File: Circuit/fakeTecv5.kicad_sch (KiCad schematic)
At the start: 33 parts, among them J11 FET1 3,3, J12 FET2 3,3, J13 FET3 3,3, J14 GPS Pins, J16 Encoder Pads, J5 I2C Oled screen, J6 FET1 Drain, J7 FET2 Drain, J8 FET3 Drain, J9 Battery Connector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

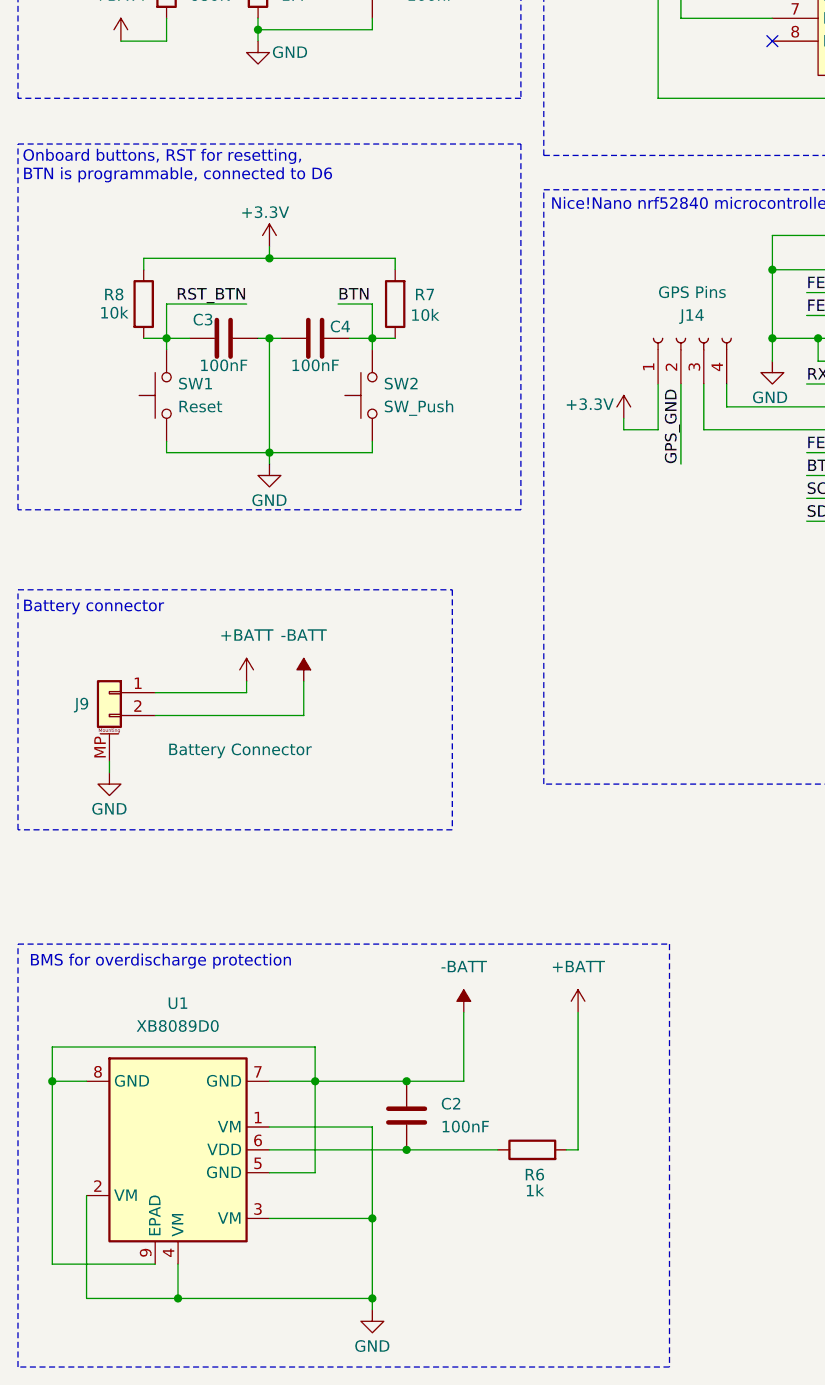
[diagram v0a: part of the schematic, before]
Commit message: Added pads for nice!nano and nrf promicro, more deco, more justifications
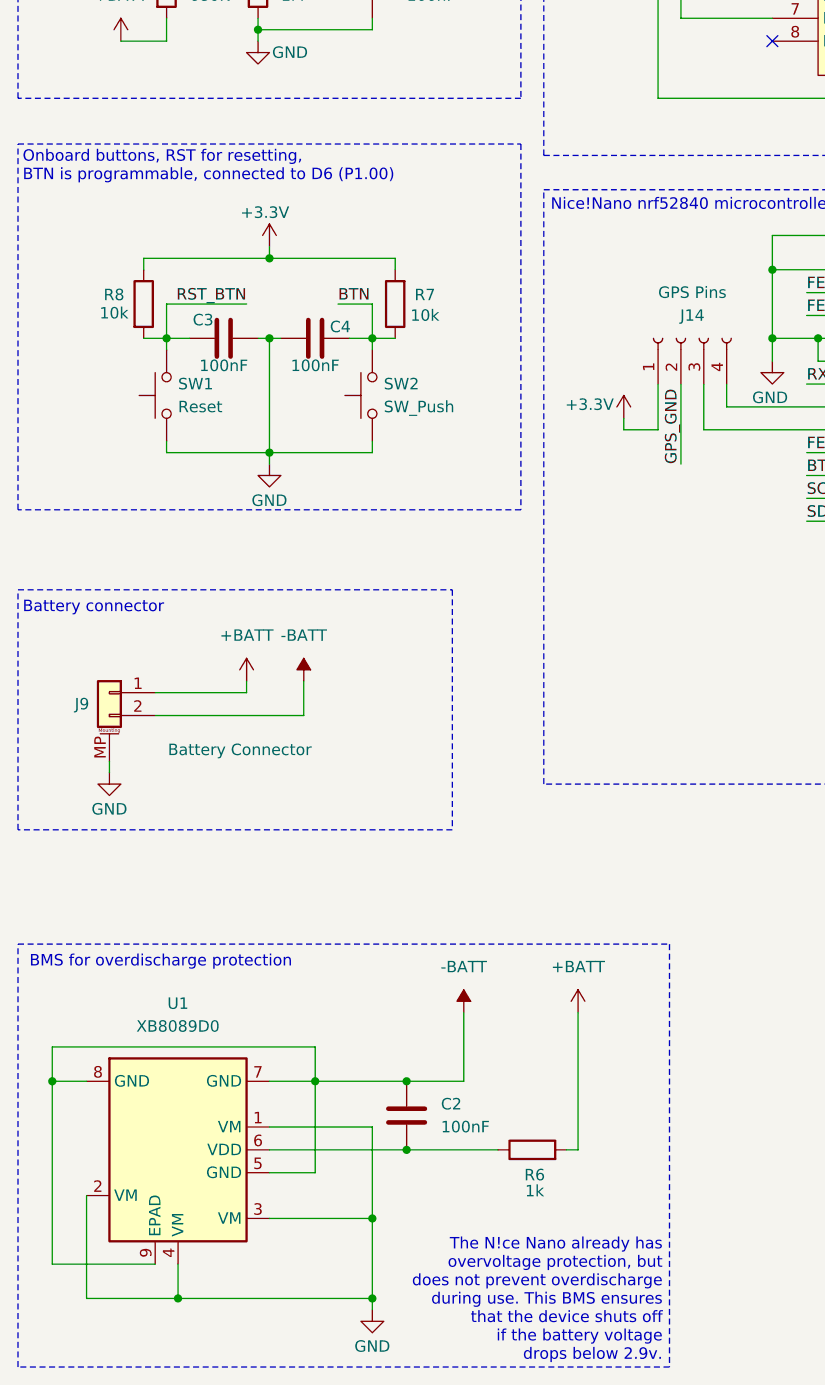
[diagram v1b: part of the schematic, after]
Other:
- note added: "Onboard buttons, RST for resetting, BTN is programmable, connected to D6 (P1.00)"
- note added: "The N!ce Nano already has overvoltage protection, but does not prevent overdischarge during use. This BMS ensures that the device shuts off if the battery voltage drops below 2.9v."
- note removed: "Onboard buttons, RST for resetting, BTN is programmable, connected to D6"
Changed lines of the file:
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@@
+		)
+	)
+	(text "The N!ce Nano already has\novervoltage protection, but\ndoes not prevent overdischarge\nduring use. This BMS ensures\nthat the device shuts off \nif the battery voltage \ndrops below 2.9v."
+		(exclude_from_sim no)
+		(at 90.678 189.992 0)
+		(effects
+			(font
+				(size 1.27 1.27)
+			)
+			(justify right bottom)
 		)
 	)
@@
 		)
 	)
-	(text "Onboard buttons, RST for resetting,\nBTN is programmable, connected to D6"
+	(text "Onboard buttons, RST for resetting,\nBTN is programmable, connected to D6 (P1.00)"
 		(exclude_from_sim no)
 		(at 19.558 57.15 0)

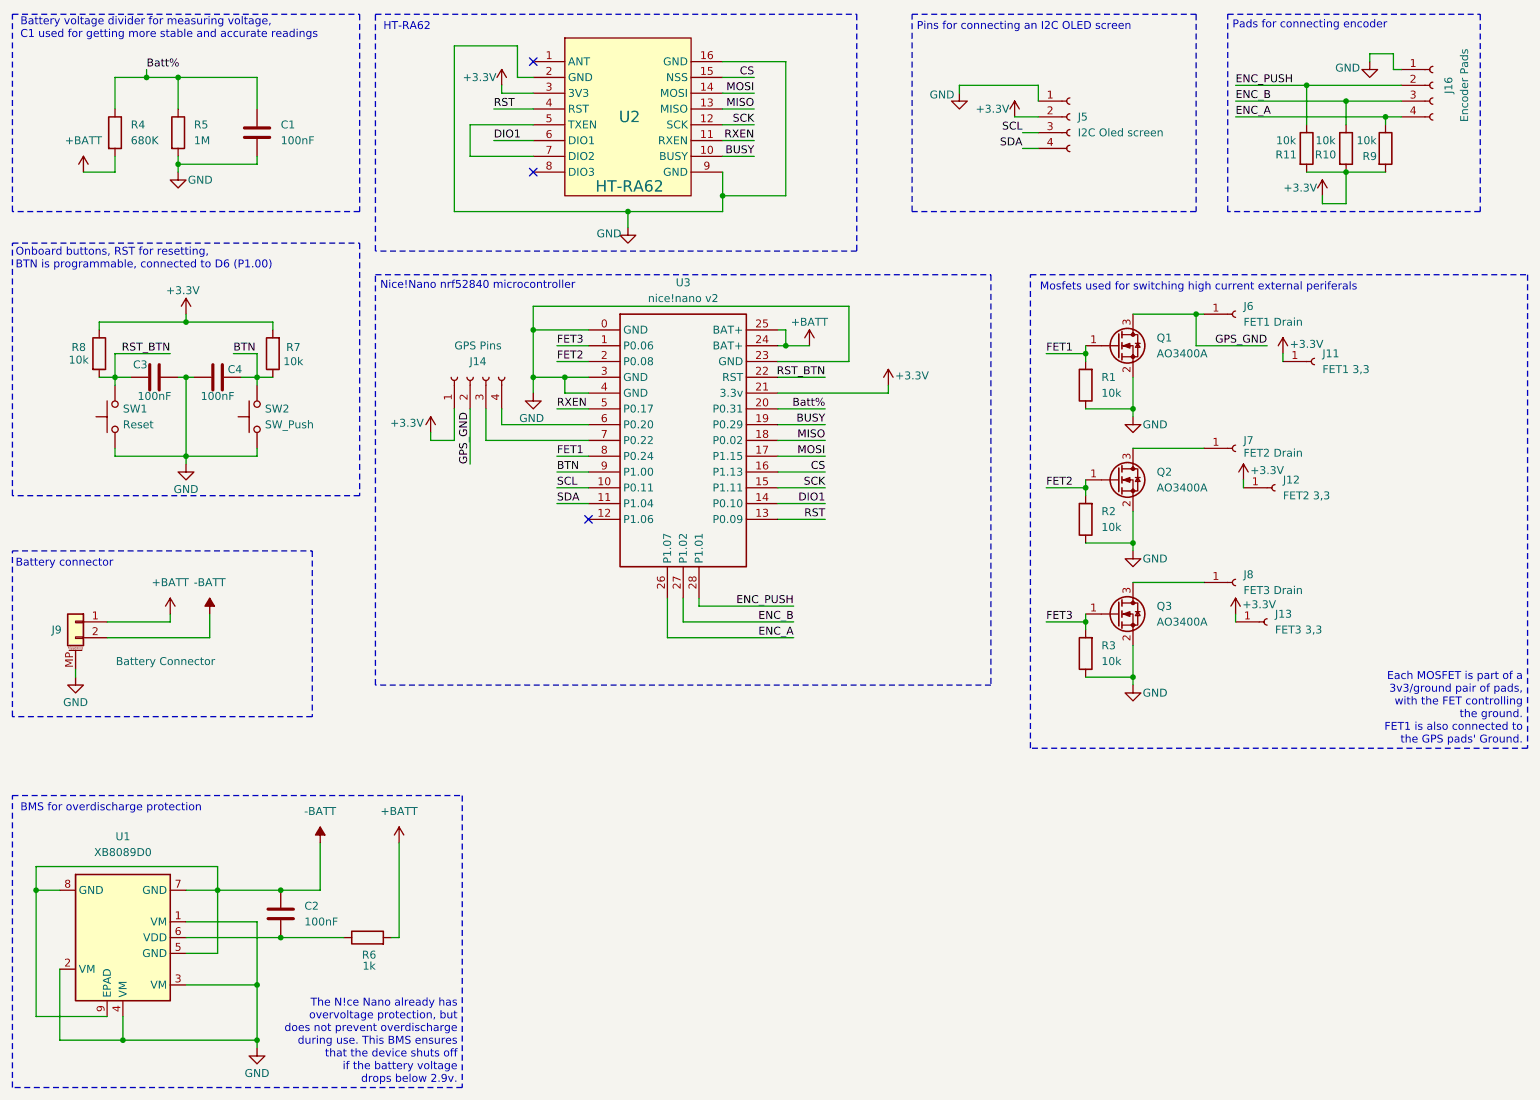
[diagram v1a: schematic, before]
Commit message: Added space to edge of board, removed pull up resistors and debouncing capacitors, added access to extra pin
Inspiration taken from fork: https://github.com/mofosyne/roTec_pcb.
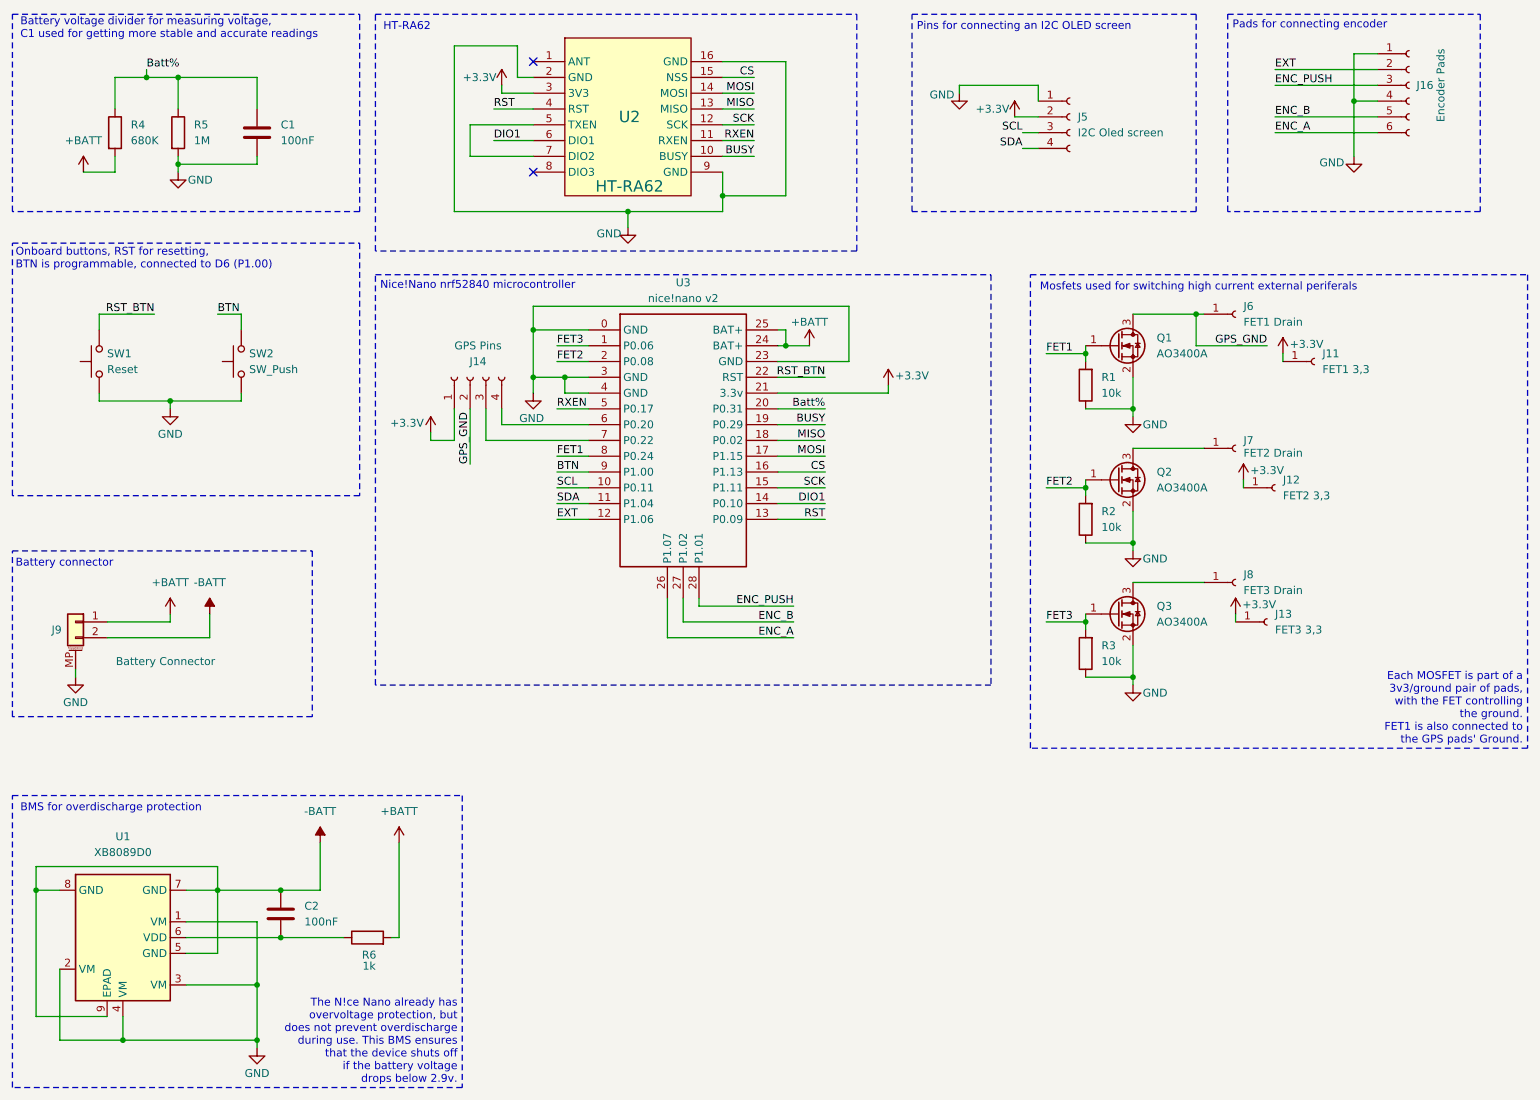
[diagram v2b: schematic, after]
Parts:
- removed C3, C4: 100nF, Capacitor_SMD:C_0805_2012Metric_Pad1.18x1.45mm_HandSolder, symbol Device:C
- removed R10, R11, R7, R8, R9: 10k, Resistor_SMD:R_0805_2012Metric_Pad1.20x1.40mm_HandSolder, symbol Device:R
- J16: footprint SMD_PAD:SMD_PAD_1x04 -> SMD_PAD:SMD_PAD_1x06; symbol Connector:Conn_01x04_Socket -> Connector:Conn_01x06_Socket
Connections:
- net ENC_A: now also J16.6 (Pin_6); no longer J16.4 (Pin_4)
- net ENC_B: now also J16.5 (Pin_5); no longer J16.3 (Pin_3)
- net ENC_PUSH: now also J16.3 (Pin_3); no longer J16.2 (Pin_2)
- net GND: now also J16.4 (Pin_4)
- net EXT: now reaches U3.12 (P1.06)
- net EXT: now also J16.2 (Pin_2)
- no-connect marks 3 -> 2
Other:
- moved on the sheet: SW1, SW2
